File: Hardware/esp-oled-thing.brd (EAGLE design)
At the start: 34.3 x 27 mm, 37 parts, among them Q1 2.5A/30V, U1 MCP73831, U2 TPS61200

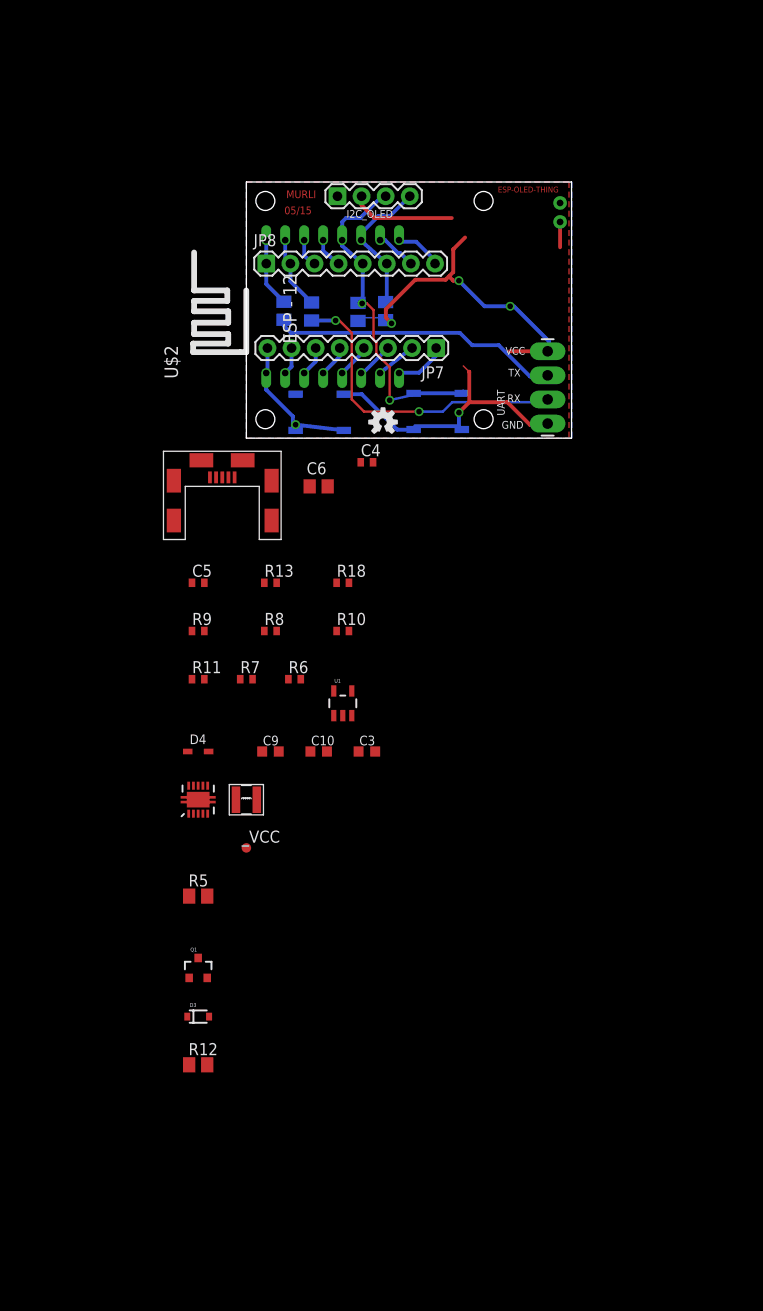
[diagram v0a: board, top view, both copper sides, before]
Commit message: TPS61200 based system power, mc73831 lipo charger added. microusb changed to a sturdier design. some more minor bug fixes in the ESP-12 section. ability to control power (enable-disable the regulator)from the ESP module.
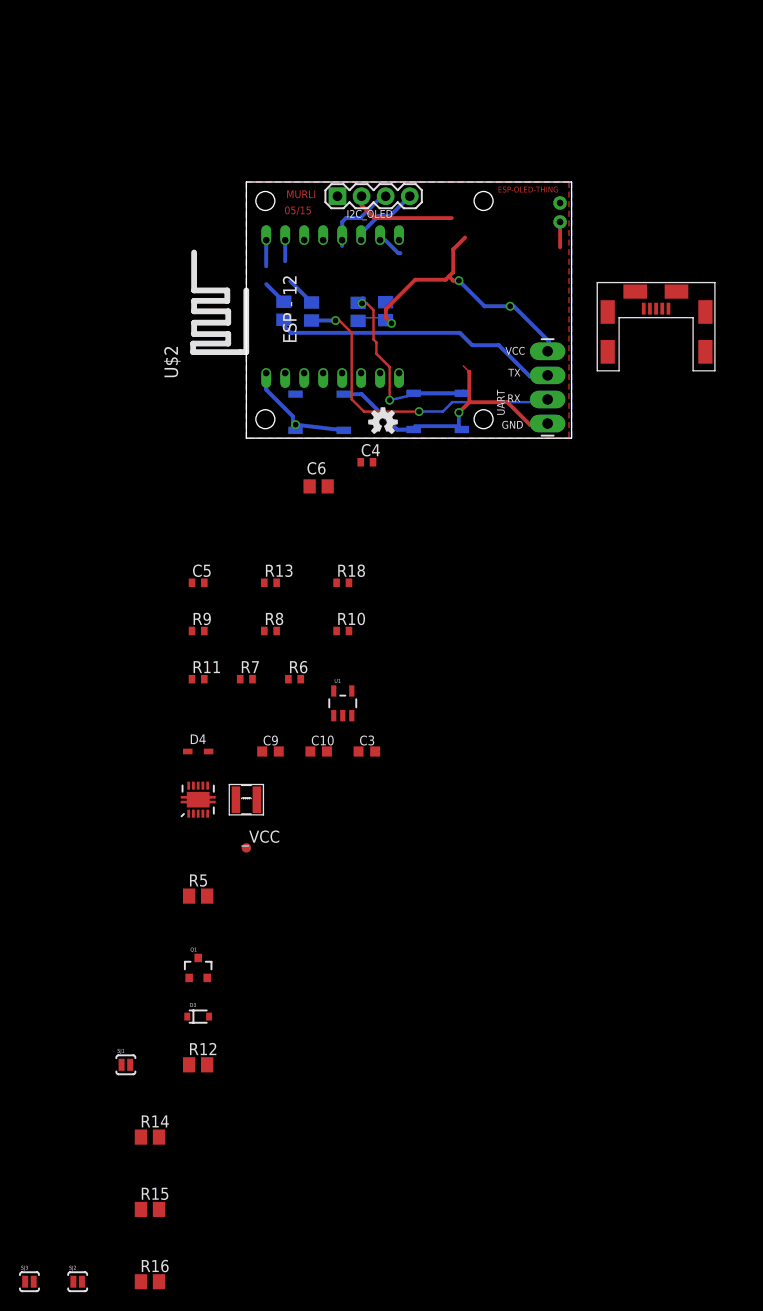
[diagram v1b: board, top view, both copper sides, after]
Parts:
- removed JP7, JP8: (no value), SparkFun:1X08
- added R14, R15: 4.7K, adafruit:M0805
- added R16: 10K, adafruit:M0805
- added SJ1, SJ2, SJ3: SOLDERJUMPERNO, SparkFun:SJ_2S-NO
- moved U$4 49.1 mm to (43.2, 12.7)
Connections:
- removed net N$11: JP8.3, U$2.GPIO4
- removed net N$12: JP8.4, U$2.GPIO5
- removed net N$16: JP8.8, U$2.GND
- removed net N$17: JP7.6, U$2.CH_PD
- removed net N$6: JP7.4, U$2.GPIO14
- removed net N$7: JP7.3, U$2.GPIO12
- removed net N$9: JP7.2, U$2.GPIO13
- removed net VBAT: JP6.2, Q1.3, R12.2
- removed net VIN1: D3.C, Q1.2
- removed net VUSB: D3.A, Q1.1
- new net N$1: SJ1.2, U$2.GPIO13
- new net N$3: R16.1, U$2.CH_PD
- new net POWERPATH_OUT: C4.1, C6.1, D3.C, Q1.2, R13.2, R7.2, U$3.P$1
- net 5VIN: now also D3.A, Q1.1, R12.2, UART.1
- net CHARGER_STATUS: now also SJ1.1
- net GND: now also R15.1, SJ3.1
- net N$15: no longer JP8.7
- net N$19: no longer JP8.1
- net N$2: now also R14.1, R15.2, U$2.ADC; no longer JP7.1, U$2.VCC
- net N$20: no longer JP8.2
- net N$5: now also SJ2.1, U$2.GPIO4; no longer JP7.5, U$2.GPIO16
- net RST: no longer JP7.8
- net SCL: no longer JP8.5
- net SDA: now also SJ3.2; no longer JP8.6
- net TPS_EN: now also SJ2.2
- net VBATT: now also JP6.2, Q1.3, R14.2; no longer C4.1, C6.1, R13.2, R7.2, U$3.P$1
- net VCC: now also R16.2, U$2.VCC; no longer JP7.7, U$2.ADC, UART.1
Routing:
- net SDA: track 15.3 -> 7.71 mm
- net VCC: track 51.7 -> 44.6 mm
- net SCL: track 36.5 -> 29.9 mm
- net N$16: track 5.80 -> 0.00 mm
- net N$2: track 5.47 -> 0.00 mm
- net N$9: track 4.28 -> 0.00 mm
- net N$7: track 3.92 -> 0.00 mm
- net N$6: track 3.58 -> 0.00 mm
- net N$5: track 3.35 -> 0.00 mm
- net N$12: track 3.24 -> 0.00 mm
- net N$17: track 3.13 -> 0.00 mm
- net N$11: track 3.03 -> 0.00 mm
- net RST: track 15.1 -> 12.6 mm
- net N$20: track 7.85 -> 5.37 mm
- net N$19: track 7.84 -> 5.38 mm
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
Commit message: minor shchematic changes, initial board layout started.
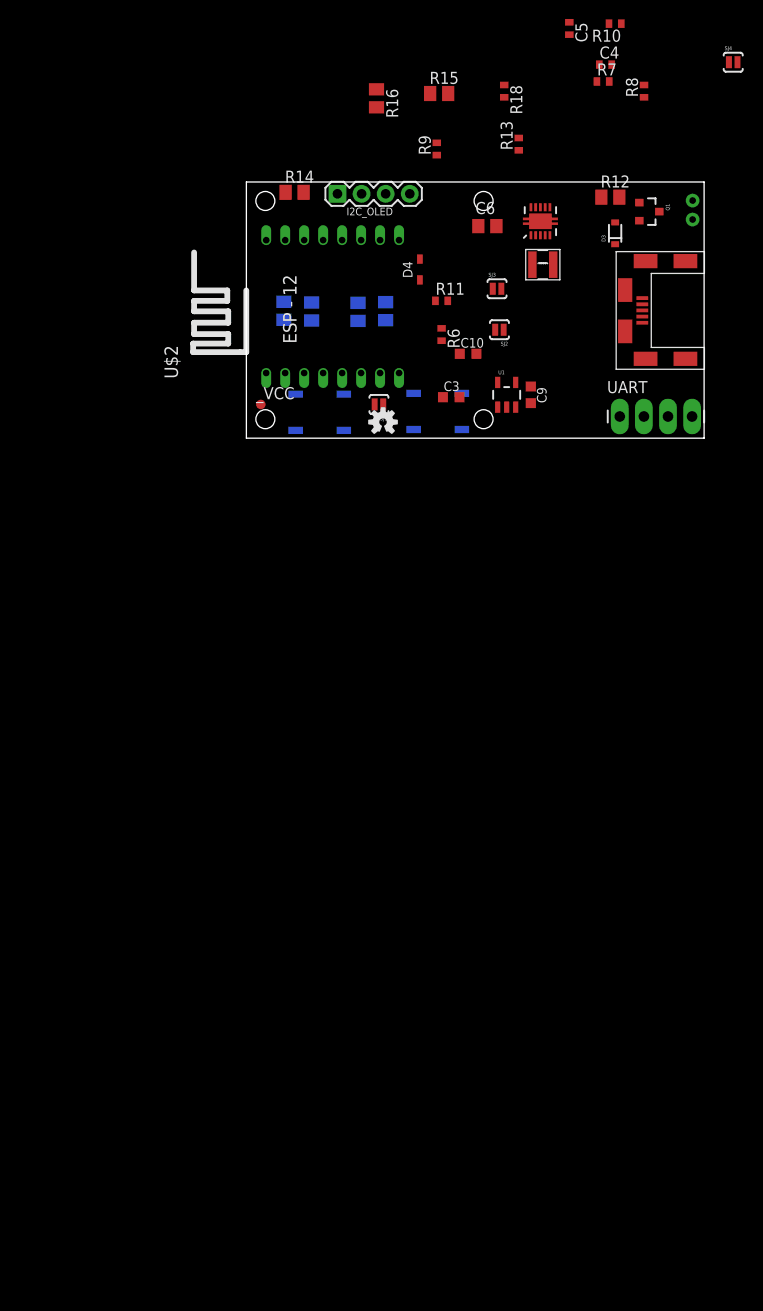
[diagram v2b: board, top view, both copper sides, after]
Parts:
- removed R5: 0Ohm, adafruit:M0805
- added SJ4: SOLDERJUMPERNO, SparkFun:SJ_2S-NO
- moved R16 127.0 mm to (13.7, 35.8), turned to 270 degrees
- moved R15 121.5 mm to (20.3, 36.3)
- moved SJ3 115.7 mm to (26.4, 15.7)
- moved SJ2 109.7 mm to (26.7, 11.4), turned to 180 degrees
- moved R12 101.2 mm to (38.4, 25.4)
- moved R14 100.7 mm to (5.08, 25.9)
- moved D3 93.5 mm to (38.9, 21.6), turned to 90 degrees
- moved Q1 92.8 mm to (42.4, 23.9), turned to 270 degrees
- moved SJ1 74.5 mm to (14.0, 3.56), turned to 180 degrees
- moved R7 73.4 mm to (37.6, 37.6)
- moved U2 70.8 mm to (31.0, 22.9)
- moved C5 70.3 mm to (34.0, 43.2), turned to 270 degrees
- moved R10 70.1 mm to (38.9, 43.7), turned to 180 degrees
- moved R8 69.2 mm to (41.9, 36.6), turned to 90 degrees
- moved U$3 64.5 mm to (31.2, 18.3)
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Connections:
- removed net N$15: R5.2, U$2.GPIO15
- net GND: now also SJ4.1, U$2.GPIO15; no longer R5.1
- net GND1: now also SJ4.2
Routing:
- net VCC: track 44.6 -> 0.00 mm, vias 3 -> 0
- net GND: track 34.2 -> 0.00 mm, vias 1 -> 0
- net N$8: track 33.5 -> 0.00 mm, vias 2 -> 0
- net N$4: track 30.7 -> 0.00 mm
- net SCL: track 29.9 -> 0.00 mm, vias 2 -> 0
- net RST: track 12.6 -> 0.00 mm, vias 1 -> 0
- net SDA: track 7.71 -> 0.00 mm
- net N$19: track 5.38 -> 0.00 mm
- net N$20: track 5.37 -> 0.00 mm
- net N$15: track 2.72 -> 0.00 mm
- removed copper zone on layer 16, net GND
- removed copper zone on layer 1, net N$13
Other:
- board size 34.3 x 27 mm -> 48.2 x 27 mm
- board text removed: "05/15"
- board text removed: "ESP-OLED-THING"
- board text removed: "GND"
- board text removed: "MURLI"
- board text removed: "RX"
- board text removed: "TX"
- board text removed: "VCC"

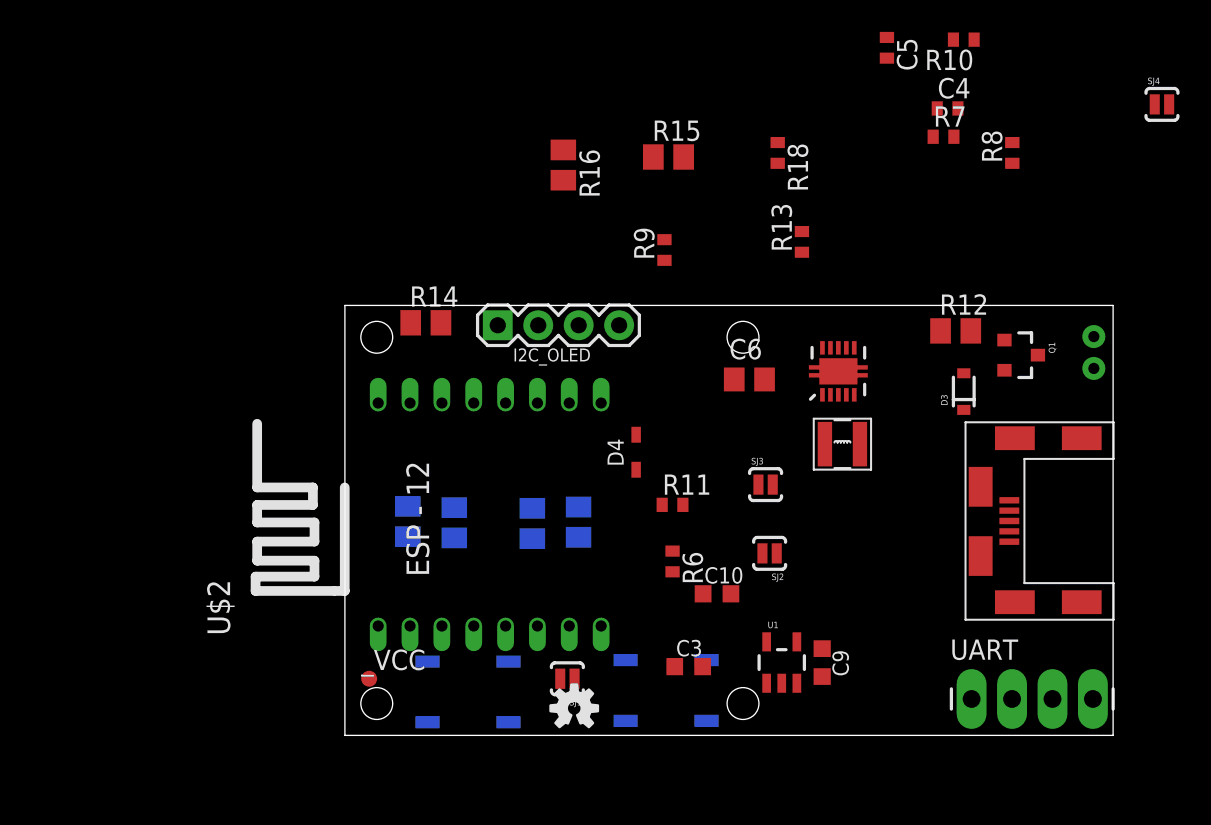
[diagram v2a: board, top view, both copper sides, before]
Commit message: minor layout modifications
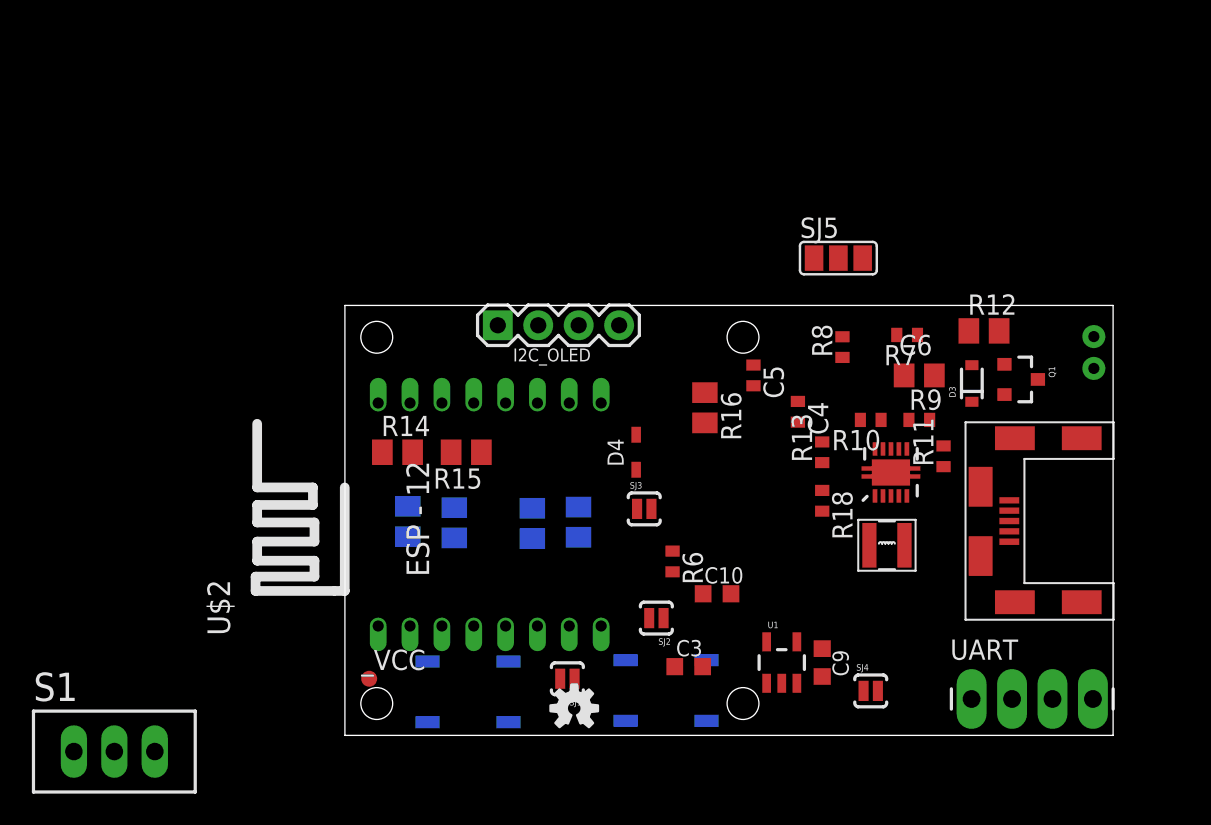
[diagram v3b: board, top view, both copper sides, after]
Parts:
- added S1: TL39PO, switch:TL3XPO
- added SJ5: (no value), jumper:SJ_2
- moved SJ4 41.1 mm to (33.0, 2.79)
- moved R10 24.6 mm to (33.0, 19.8)
- moved R15 22.5 mm to (7.62, 17.8), turned to 180 degrees
- moved C5 22.2 mm to (25.7, 22.6)
- moved R18 22.0 mm to (30.0, 14.7)
- moved C4 21.2 mm to (28.4, 20.3), turned to 270 degrees
- moved R9 19.2 mm to (36.1, 19.8), turned to 0 degrees
- moved R16 17.6 mm to (22.6, 20.6)
- moved R11 17.3 mm to (37.6, 17.5), turned to 90 degrees
- moved R8 16.2 mm to (31.2, 24.4)
- moved R13 13.3 mm to (30.0, 17.8)
- moved R7 12.7 mm to (35.3, 25.1), turned to 180 degrees
- moved C6 10.7 mm to (36.1, 22.6)
- moved R14 8.32 mm to (3.30, 17.8)
- moved SJ2 8.19 mm to (19.6, 7.37)
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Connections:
- new net SYSPOWER_IN: C4.1, C6.1, R13.2, R7.2, SJ5.2, U$3.P$1
- net POWERPATH_OUT: now also SJ5.3; no longer C4.1, C6.1, R13.2, R7.2, U$3.P$1
- net TPS_EN: now also S1.2
- net VBATT: now also SJ5.1
- net VCC: now also S1.1

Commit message: more layout changes
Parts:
- moved S1 32.2 mm to (4.57, 24.9)
- moved R14 18.6 mm to (21.8, 16.3)
- moved R15 14.7 mm to (21.8, 14.0)
- moved C3 13.3 mm to (34.0, 8.89)
- moved C5 11.5 mm to (30.5, 12.2), turned to 180 degrees
- moved SJ5 8.39 mm to (24.1, 25.1)
- moved SJ3 7.89 mm to (19.3, 22.1)
- moved D4 4.37 mm to (21.8, 20.3)
- moved R16 2.05 mm to (24.6, 20.3)
- moved I2C_OLED 1.83 mm to (11.1, 24.7)

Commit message: Initial layout started.
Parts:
- removed SJ1, SJ2, SJ3, SJ4: SOLDERJUMPERNO, SparkFun:SJ_2S-NO
- added CHARGER_STATUS, GPIO2_GND, SMPS_GND, TPS_EN: SOLDERJUMPERNO, SparkFun:SJ_2S-NO
- added GND: TPTP10R, testpad:TP10R
- moved _VCC 34.4 mm to (27.4, 26.2)
- moved SJ5 19.8 mm to (34.3, 8.13)
- moved C3 11.3 mm to (27.4, 18.0), turned to 270 degrees
- moved R13 8.41 mm to (37.3, 13.7), turned to 270 degrees
- moved C4 7.64 mm to (36.1, 19.8), turned to 0 degrees
- moved R9 5.43 mm to (30.7, 18.8), turned to 270 degrees
- moved R8 3.75 mm to (33.0, 21.1), turned to 180 degrees
- moved C9 3.56 mm to (30.0, 8.13)
- moved U1 3.31 mm to (27.2, 7.87)
- moved C5 2.81 mm to (30.7, 15.0), turned to 90 degrees
- moved R18 2.55 mm to (27.4, 14.5), turned to 90 degrees
- moved R12 1.55 mm to (41.7, 25.1)
- moved C10 0.80 mm to (23.6, 9.65)
- moved S1 0.72 mm to (5.08, 24.4), flipped to the bottom, turned to 180 degrees
- moved Q1 0.57 mm to (42.9, 22.1)
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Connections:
- net CHARGER_STATUS: now also CHARGER_STATUS.1; no longer SJ1.1
- net GND: now also GND.TP, GPIO2_GND.1, SMPS_GND.1; no longer SJ3.1, SJ4.1
- net GND1: now also SMPS_GND.2; no longer SJ4.2
- net N$1: now also CHARGER_STATUS.2; no longer SJ1.2
- net N$5: now also TPS_EN.1; no longer SJ2.1
- net SDA: now also GPIO2_GND.2; no longer SJ3.2
- net TPS_EN: now also TPS_EN.2; no longer SJ2.2
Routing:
- net SYSPOWER_IN: track 0.00 -> 18.5 mm
- net GND: track 0.00 -> 15.2 mm
- net 5VIN: track 0.00 -> 6.20 mm
- net FB: track 0.00 -> 4.22 mm
- net GND1: track 0.00 -> 3.65 mm
- net N$14: track 0.00 -> 3.45 mm
- net UVLO: track 0.00 -> 3.22 mm
- net N$18: track 0.00 -> 2.85 mm
- net VIN: track 0.00 -> 2.33 mm
- net TPS_EN: track 0.00 -> 2.06 mm
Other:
- board size 48.2 x 27 mm -> 48.3 x 27 mm

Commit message: power regulator layout done
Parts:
- moved SMPS_GND 10.2 mm to (30.2, 21.8)
- moved C9 5.59 mm to (24.4, 8.13), turned to 90 degrees
- moved C10 2.05 mm to (24.6, 11.4)
- moved R7 1.52 mm to (33.8, 25.1), turned to 0 degrees
- moved R8 0.51 mm to (33.0, 21.6)
- moved C5 0.36 mm to (31.0, 15.2)
- moved U1 0.25 mm to (27.4, 7.87), turned to 180 degrees
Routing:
- net VCC: track 0.00 -> 29.9 mm
- net GND: track 15.2 -> 33.6 mm, vias 0 -> 2
- net N$13: track 0.00 -> 16.9 mm
- net 5VIN: track 6.20 -> 21.6 mm
- net N$21: track 0.00 -> 11.4 mm
- net UVLO: track 3.22 -> 12.5 mm, vias 0 -> 3
- net VBATT: track 0.00 -> 7.74 mm
- net GND1: track 3.65 -> 8.46 mm
- net SYSPOWER_IN: track 18.5 -> 21.4 mm
- added copper zone on layer 1, net GND
- added copper zone on layer 16, net GND
